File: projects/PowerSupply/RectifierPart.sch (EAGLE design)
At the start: 13 parts, among them X1 OUT, X2 IN

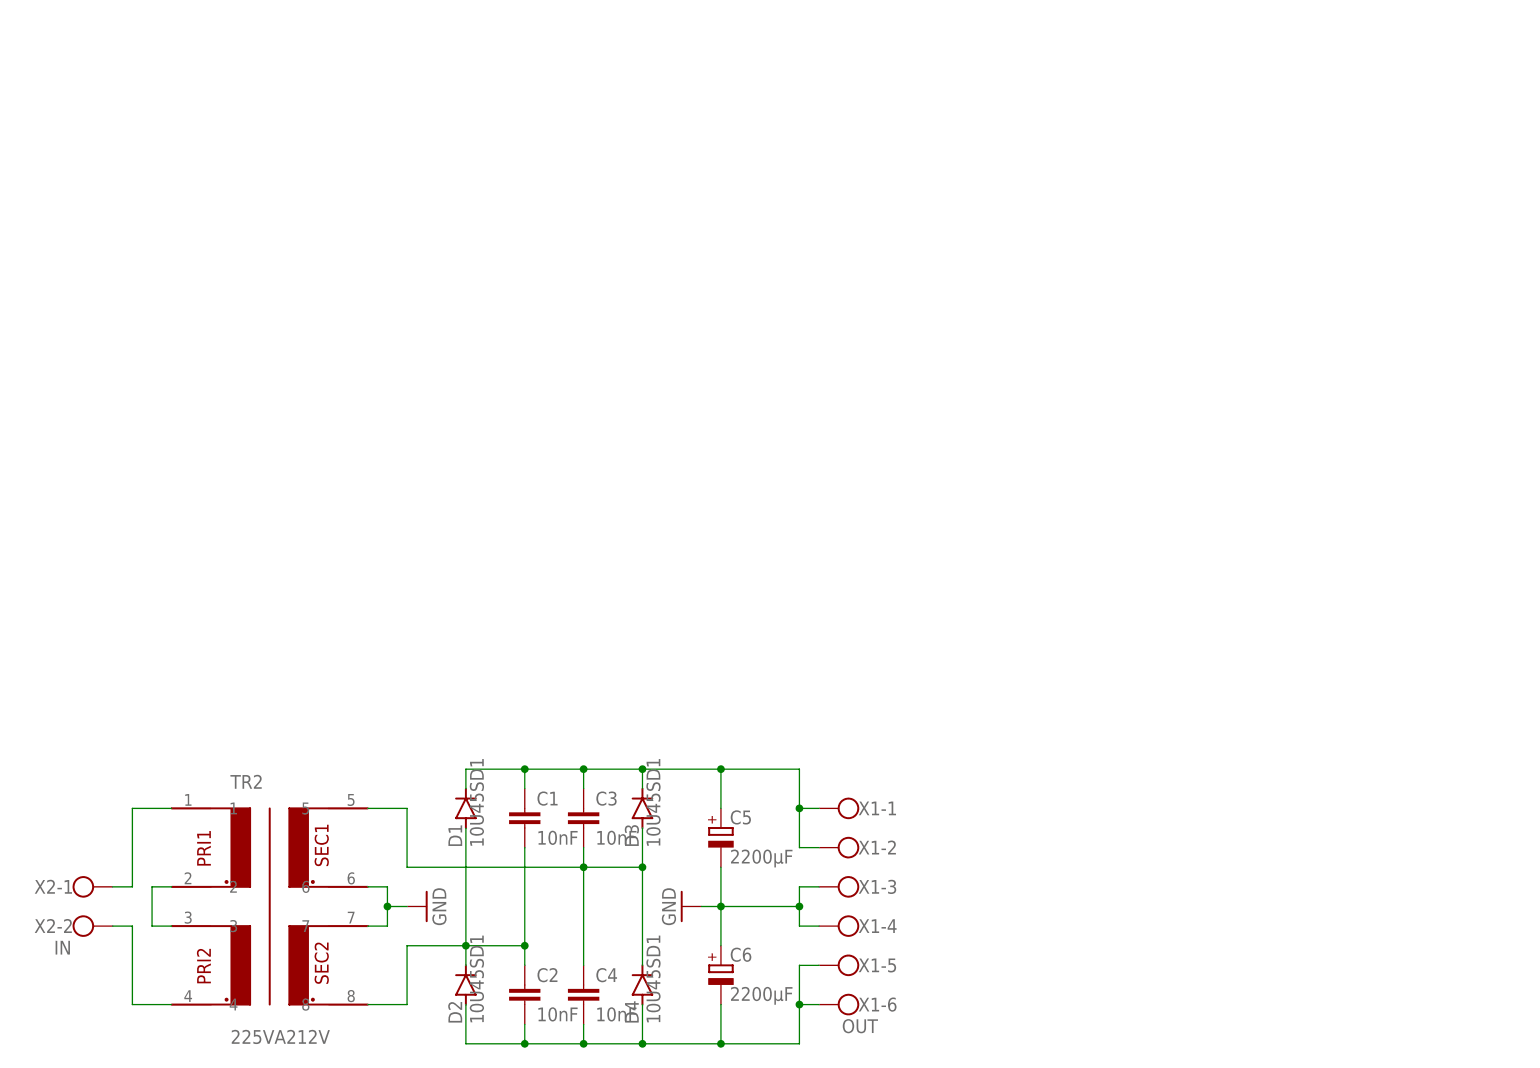
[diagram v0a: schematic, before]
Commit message: feat: power supply
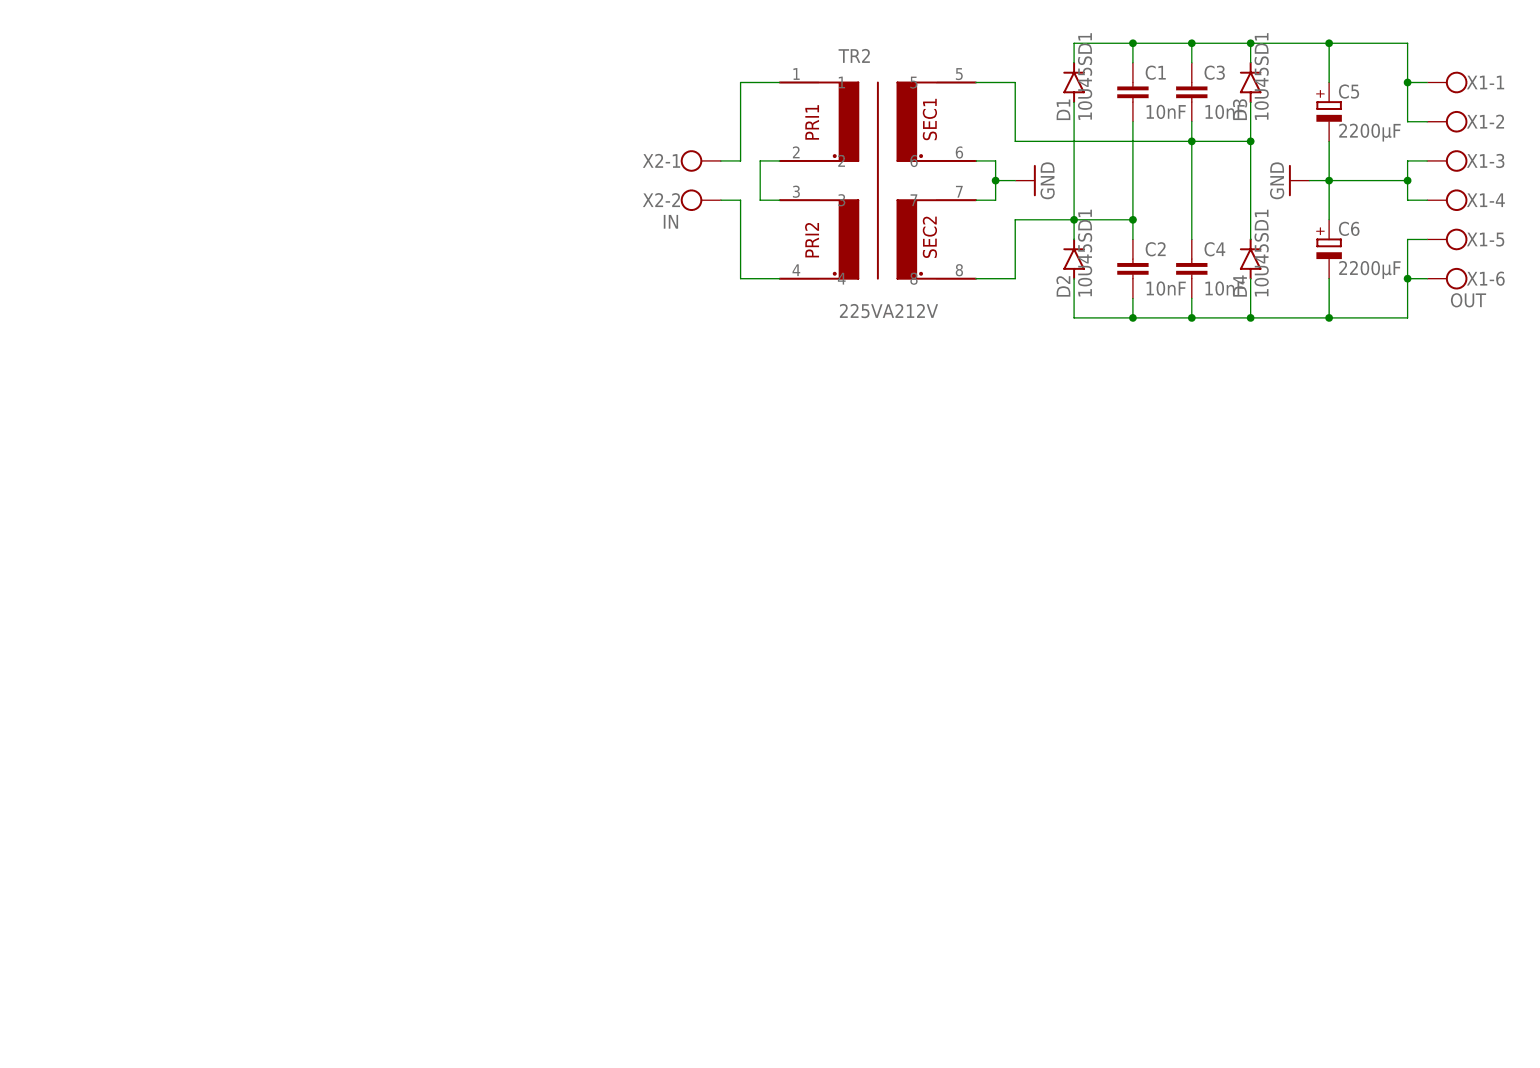
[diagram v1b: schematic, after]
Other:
- moved on the sheet: C1, C2, C3, C4, C5, C6, D1, D2, D3, D4, TR2, X1-1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
